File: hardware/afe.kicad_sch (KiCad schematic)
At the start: 39 parts, among them J2 Conn_01x02_Pin, U2 MCP6002-xMC, U3 4052

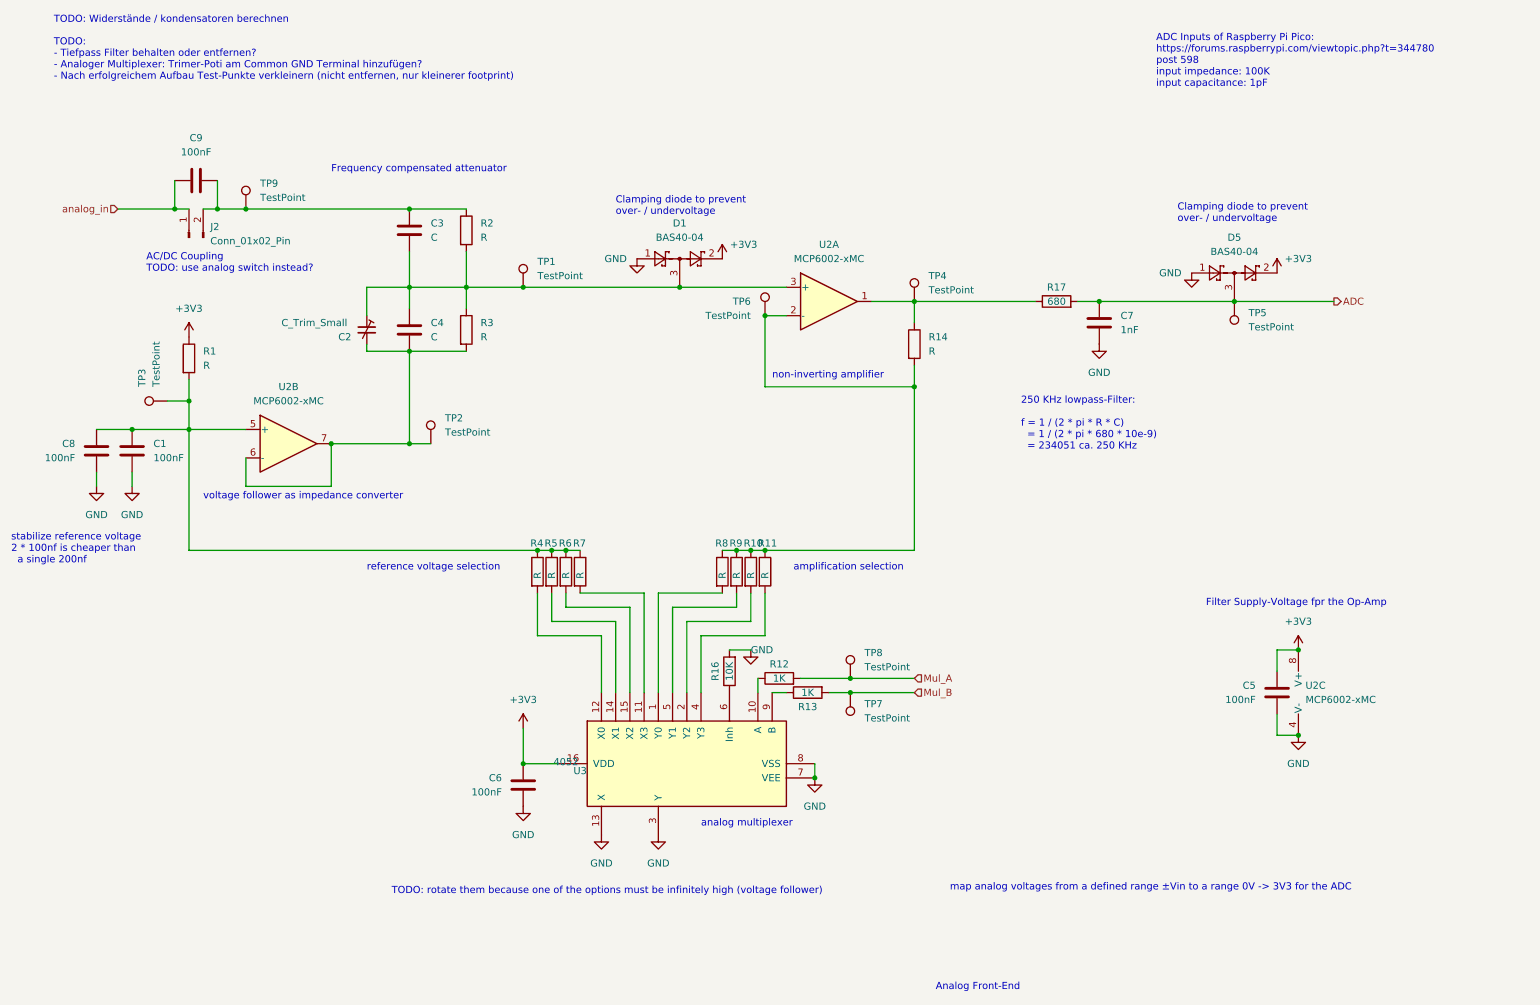
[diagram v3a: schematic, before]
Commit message: [hw] afe: reoriented mux so a high-impedance option is available for op-amp 2
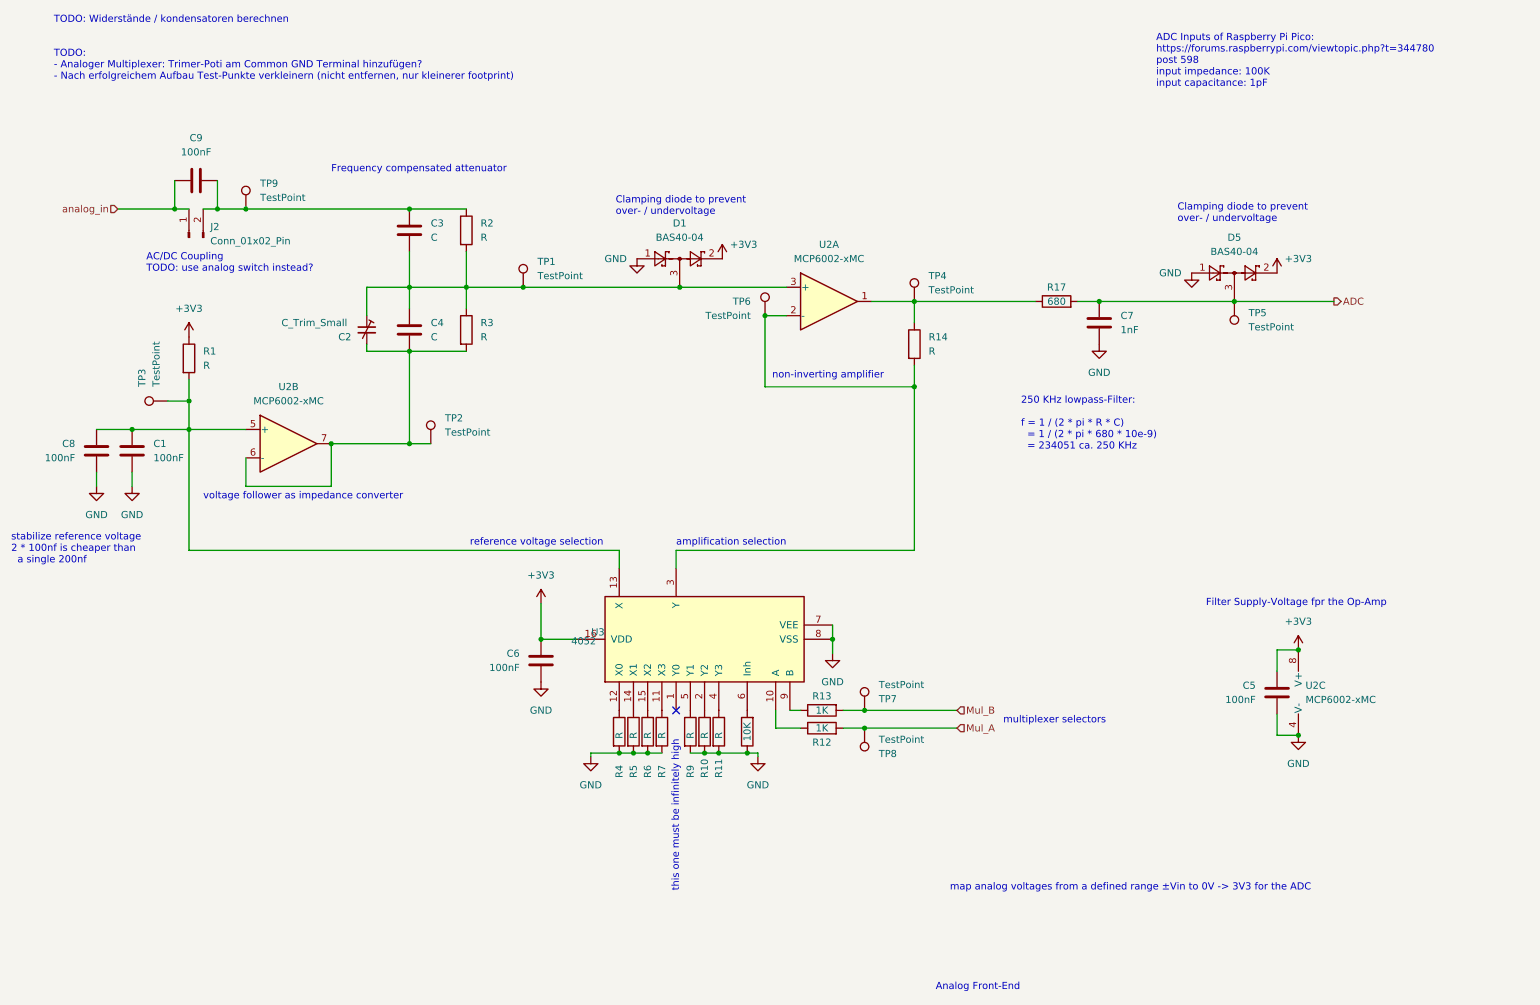
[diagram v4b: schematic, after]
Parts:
- removed R8: R, Resistor_SMD:R_0805_2012Metric_Pad1.20x1.40mm_HandSolder, symbol Device:R
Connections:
- net GND: now also R10.2, R11.2, R16.1, R4.2, R5.2, R6.2, R7.2, R9.2; no longer R16.2, U3.13 (X), U3.3 (Y)
- net at C1.1, C8.1, R1.2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: now also U3.13 (X); no longer R4.1, R5.1, R6.1, R7.1
- net at U3.11 (X3): now also R7.1; no longer R7.2
- net at U3.14 (X1): now also R5.1; no longer R5.2
- net at U3.15 (X2): now also R6.1; no longer R6.2
- net at U3.12 (X0): now also R4.1; no longer R4.2
- net at U3.2 (Y2): now also R10.1; no longer R10.2
- net at U3.4 (Y3): now also R11.1; no longer R11.2
- net at U3.5 (Y1): now also R9.1; no longer R9.2
- net at U3.6 (Inh): now also R16.2; no longer R16.1
- net at R14.2, TP6.1, U2.2 (-): now also U3.3 (Y); no longer R10.1, R11.1, R9.1
- no-connect marks 0 -> 1
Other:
- note added: "TODO: - Analoger Multiplexer: Trimer-Poti am Common GND Terminal hinzufügen? - Nach erfolgreichem Aufbau Test-Punkte verkleinern (nicht entfernen, nur kleinerer footprint)"
- note added: "map analog voltages from a defined range ±Vin to 0V -> 3V3 for the ADC"
- note added: "multiplexer selectors"
- note added: "this one must be infinitely high"
- note removed: "TODO: - Tiefpass Filter behalten oder entfernen? - Analoger Multiplexer: Trimer-Poti am Common GND Terminal hinzufügen? - Nach erfolgreichem Aufbau Test-Punkte verkleinern (nicht entfernen, nur kleinerer footprint)"
- note removed: "TODO: rotate them because one of the options must be infinitely high (voltage follower)"
- note removed: "analog multiplexer"
- note removed: "map analog voltages from a defined range ±Vin to a range 0V -> 3V3 for the ADC"
- moved on the sheet: C6, R12, R13, TP7, TP8, U3

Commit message: update analog front-end and resistor calculator: Better documentation
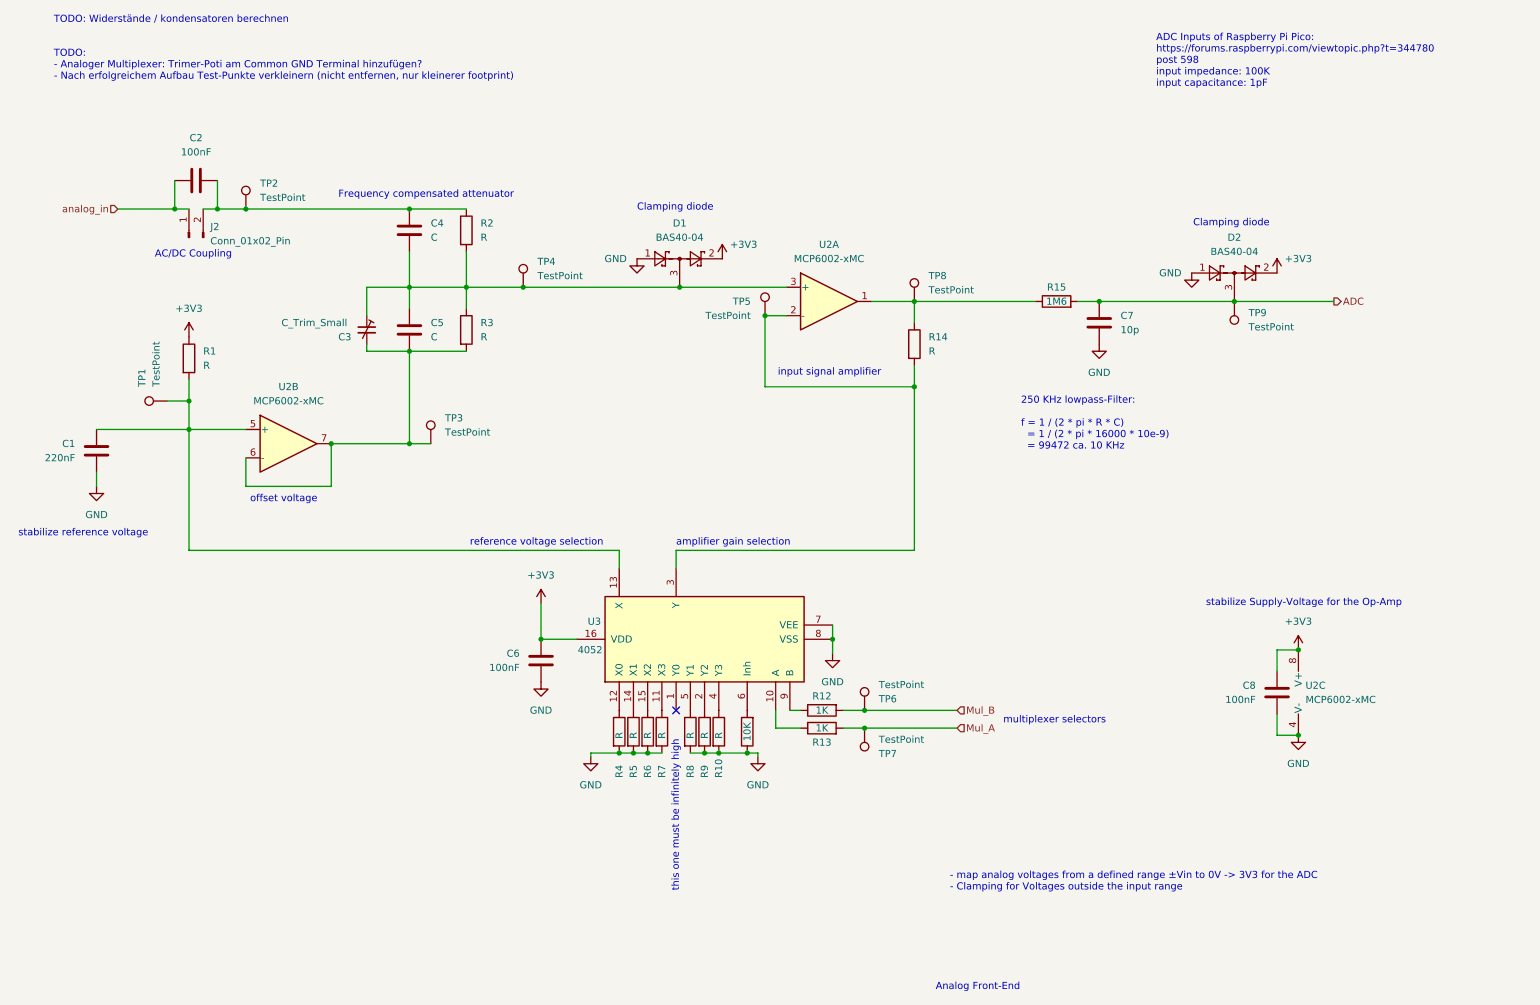
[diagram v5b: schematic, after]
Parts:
- removed C1: 100nF, Capacitor_SMD:C_0805_2012Metric_Pad1.18x1.45mm_HandSolder, symbol Device:C
- C1: renamed from C8; value 100nF -> 220nF; footprint Capacitor_SMD:C_0805_2012Metric_Pad1.18x1.45mm_HandSolder -> Capacitor_SMD:C_0603_1608Metric
- C2: renamed from C9; footprint Capacitor_SMD:C_0805_2012Metric_Pad1.18x1.45mm_HandSolder -> Capacitor_SMD:C_0603_1608Metric
- C4: renamed from C3; footprint Capacitor_SMD:C_0805_2012Metric_Pad1.18x1.45mm_HandSolder -> Capacitor_SMD:C_0603_1608Metric
- C5: renamed from C4; footprint Capacitor_SMD:C_0805_2012Metric_Pad1.18x1.45mm_HandSolder -> Capacitor_SMD:C_0603_1608Metric
- C6: footprint Capacitor_SMD:C_0805_2012Metric_Pad1.18x1.45mm_HandSolder -> Capacitor_SMD:C_0603_1608Metric
- C7: value 1nF -> 10p; footprint Capacitor_SMD:C_0805_2012Metric_Pad1.18x1.45mm_HandSolder -> Capacitor_SMD:C_0603_1608Metric
- C8: renamed from C5; footprint Capacitor_SMD:C_0805_2012Metric_Pad1.18x1.45mm_HandSolder -> Capacitor_SMD:C_0603_1608Metric
- R1, R14, R2, R3, R4, R5, R6, R7: footprint Resistor_SMD:R_0805_2012Metric_Pad1.20x1.40mm_HandSolder -> Resistor_SMD:R_0603_1608Metric
- R10: renamed from R11; footprint Resistor_SMD:R_0805_2012Metric_Pad1.20x1.40mm_HandSolder -> Resistor_SMD:R_0603_1608Metric
- R11: renamed from R16; footprint Resistor_SMD:R_0805_2012Metric_Pad1.20x1.40mm_HandSolder -> Resistor_SMD:R_0603_1608Metric
- R12: renamed from R13; footprint Resistor_SMD:R_0805_2012Metric_Pad1.20x1.40mm_HandSolder -> Resistor_SMD:R_0603_1608Metric
- R13: renamed from R12; footprint Resistor_SMD:R_0805_2012Metric_Pad1.20x1.40mm_HandSolder -> Resistor_SMD:R_0603_1608Metric
- R15: renamed from R17; value 680 -> 1M6; footprint Resistor_SMD:R_0805_2012Metric_Pad1.20x1.40mm_HandSolder -> Resistor_SMD:R_0603_1608Metric
- R8: renamed from R9; footprint Resistor_SMD:R_0805_2012Metric_Pad1.20x1.40mm_HandSolder -> Resistor_SMD:R_0603_1608Metric
- R9: renamed from R10; footprint Resistor_SMD:R_0805_2012Metric_Pad1.20x1.40mm_HandSolder -> Resistor_SMD:R_0603_1608Metric
- renumbered C2 to C3, D5 to D2, TP3 to TP1, TP9 to TP2, TP2 to TP3, TP1 to TP4, TP6 to TP5, TP7 to TP6, TP8 to TP7, TP4 to TP8, TP5 to TP9
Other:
- note added: "- map analog voltages from a defined range ±Vin to 0V -> 3V3 for the ADC - Clamping for Voltages outside the input range"
- note added: "250 KHz lowpass-Filter: f = 1 / (2 * pi * R * C) = 1 / (2 * pi * 16000 * 10e-9) = 99472 ca. 10 KHz"
- note added: "AC/DC Coupling"
- note added: "Clamping diode"
- note added: "amplifier gain selection"
- note added: "input signal amplifier"
- note added: "offset voltage"
- note added: "stabilize Supply-Voltage for the Op-Amp"
- note added: "stabilize reference voltage"
- note removed: "250 KHz lowpass-Filter: f = 1 / (2 * pi * R * C) = 1 / (2 * pi * 680 * 10e-9) = 234051 ca. 250 KHz"
- note removed: "AC/DC Coupling TODO: use analog switch instead?"
- note removed: "Clamping diode to prevent over- / undervoltage"
- note removed: "Filter Supply-Voltage fpr the Op-Amp"
- note removed: "amplification selection"
- note removed: "map analog voltages from a defined range ±Vin to 0V -> 3V3 for the ADC"
- note removed: "non-inverting amplifier"
- note removed: "stabilize reference voltage 2 * 100nf is cheaper than a single 200nf"
- note removed: "voltage follower as impedance converter"

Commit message: update schematics to calculated values
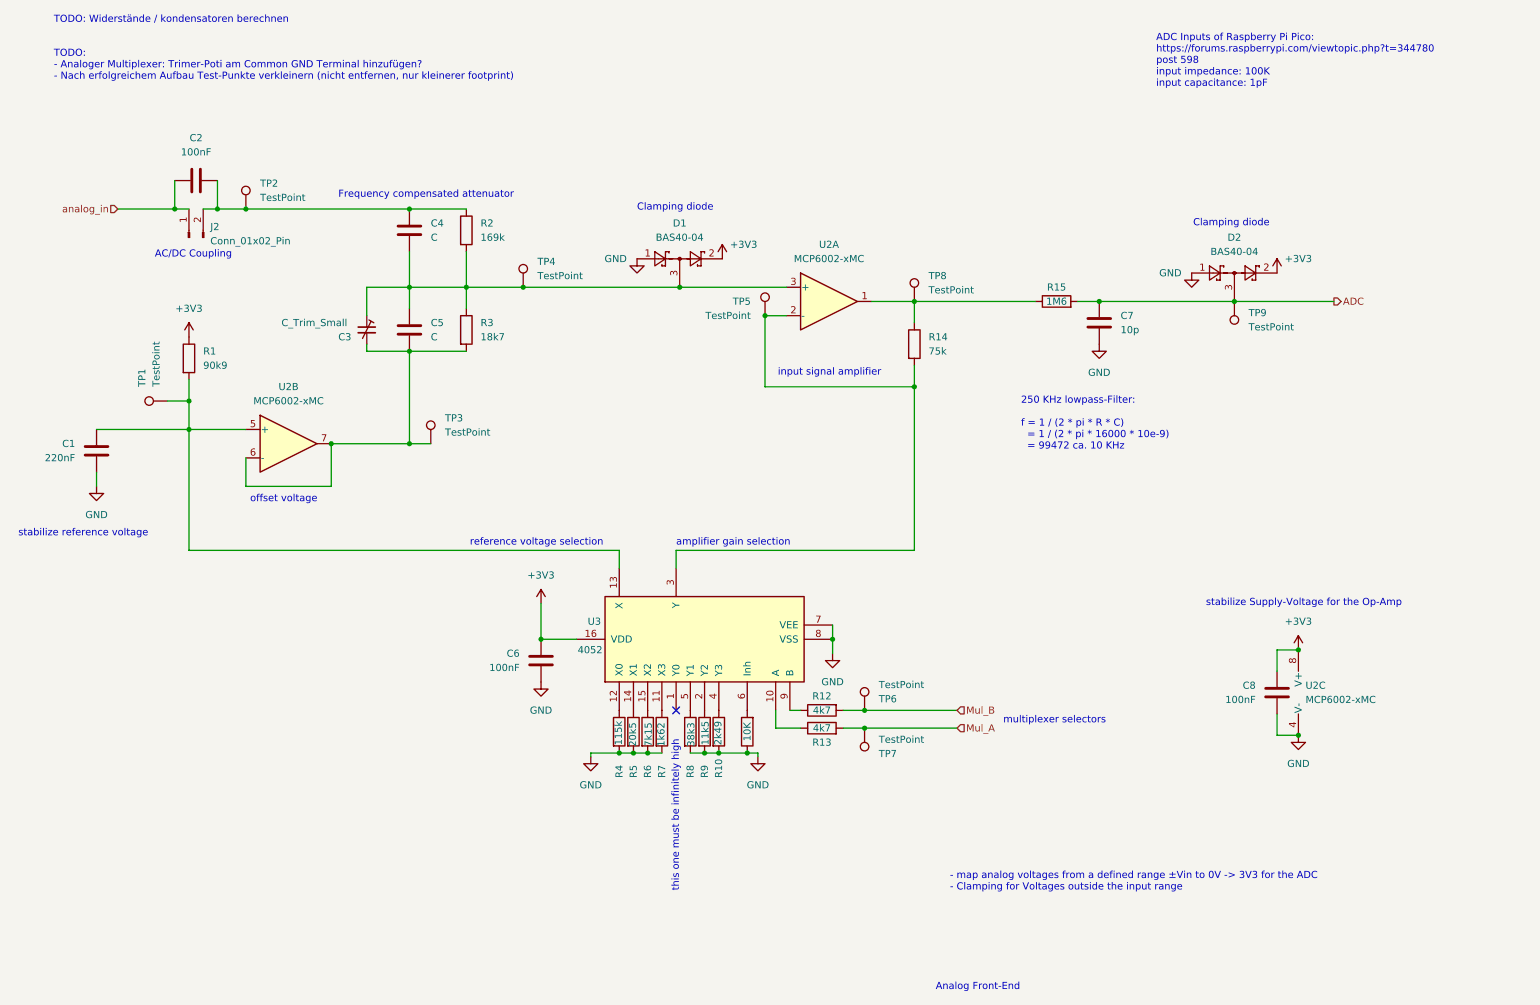
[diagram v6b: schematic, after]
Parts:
- R1: value R -> 90k9
- R10: value R -> 2k49
- R12, R13: value 1K -> 4k7
- R14: value R -> 75k
- R2: value R -> 169k
- R3: value R -> 18k7
- R4: value R -> 115k
- R5: value R -> 20k5
- R6: value R -> 7k15
- R7: value R -> 1k62
- R8: value R -> 38k3
- R9: value R -> 11k5

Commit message: afe and simulation ready
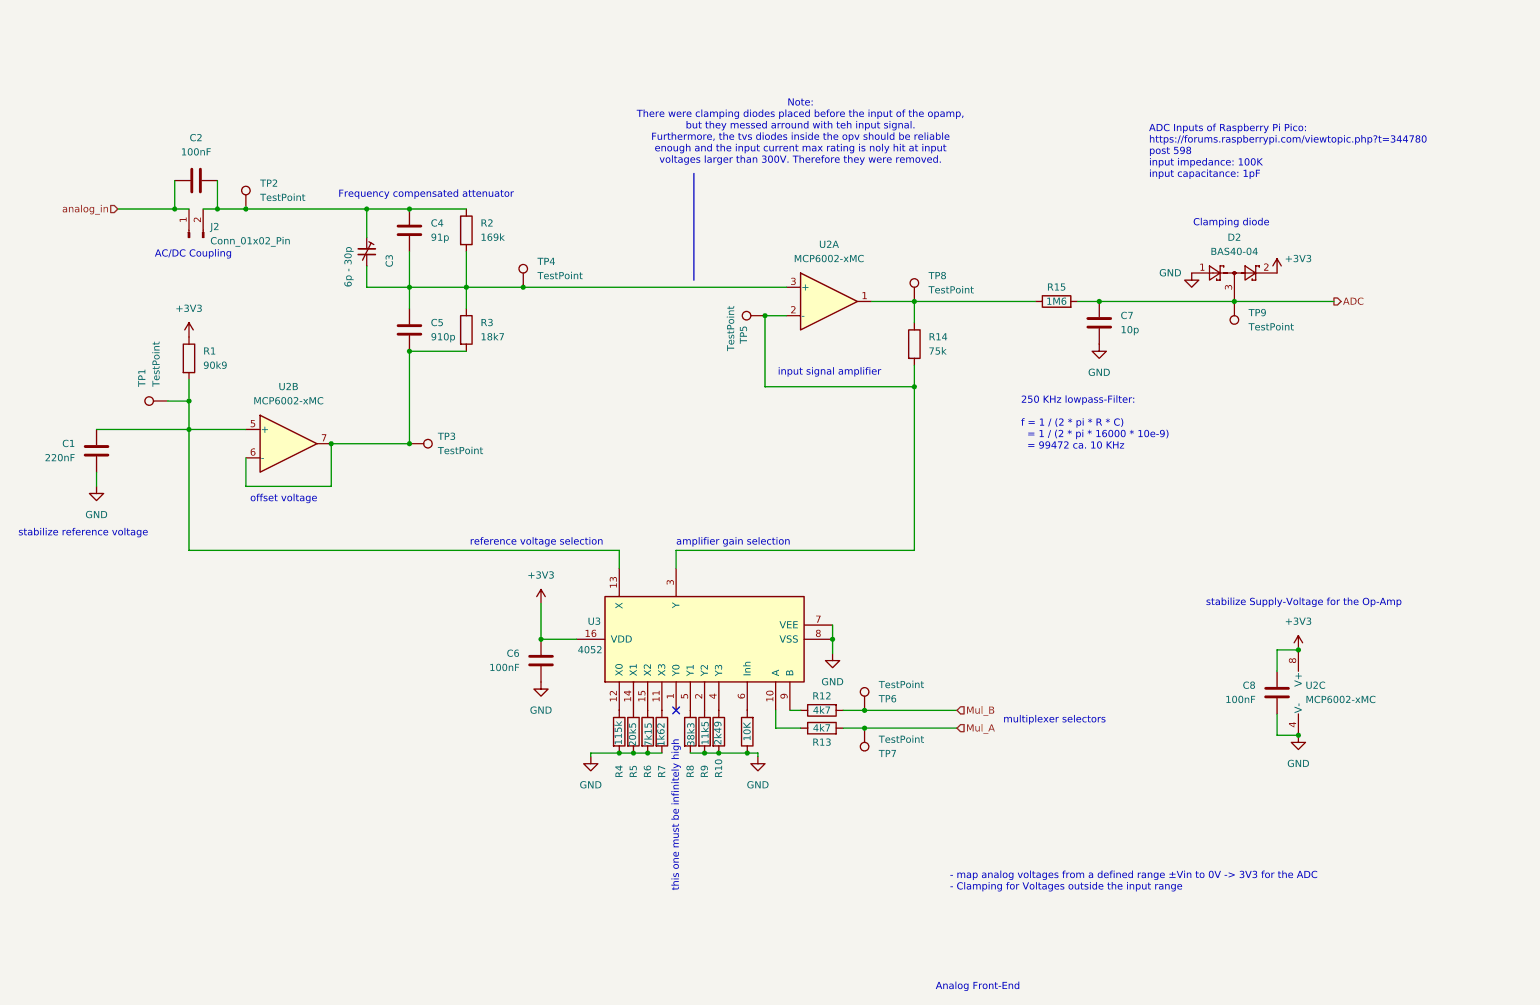
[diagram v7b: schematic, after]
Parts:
- removed D1: BAS40-04, Package_TO_SOT_SMD:SOT-23, symbol Diode:BAS40-04
- C3: value C_Trim_Small -> 6p - 30p; footprint additional_parts:c_trim_D5.08mm_P5.08mm -> additional_parts:c_trim_D6mm_P5mm_1; link (none) -> https://de.rs-online.com/web/p/variable-trimmkondensatoren/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
- C4: value C -> 91p
- C5: value C -> 910p
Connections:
- net at C5.2, R3.2, TP3.1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: no longer C3.2
- net at C2.2, C4.1, J2.2 (Pin_2)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: now also C3.1
- net at C4.2, C5.1, R2.2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: now also C3.2; no longer C3.1
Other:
- note added: "Note: There were clamping diodes placed before the input of the opamp, but they messed arround with teh input signal. Furthermore, the tvs diodes inside the opv should be reliable enough and the input current max rating is noly hit at input voltages larger than 300V. Therefore they were removed."
- note removed: "TODO: - Analoger Multiplexer: Trimer-Poti am Common GND Terminal hinzufügen? - Nach erfolgreichem Aufbau Test-Punkte verkleinern (nicht entfernen, nur kleinerer footprint)"
- note removed: "TODO: Widerstände / kondensatoren berechnen"
- moved on the sheet: C3, TP3, TP5
